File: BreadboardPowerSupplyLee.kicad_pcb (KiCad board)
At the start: 2 copper layers, 31.8 x 50.8 mm, 15 parts, among them J1 Barrel_Jack_Switch, J2 Conn_02x02_Odd_Even, J3 Conn_02x02_Odd_Even, SW1 SW_SPDT, U1 LM7805_TO220

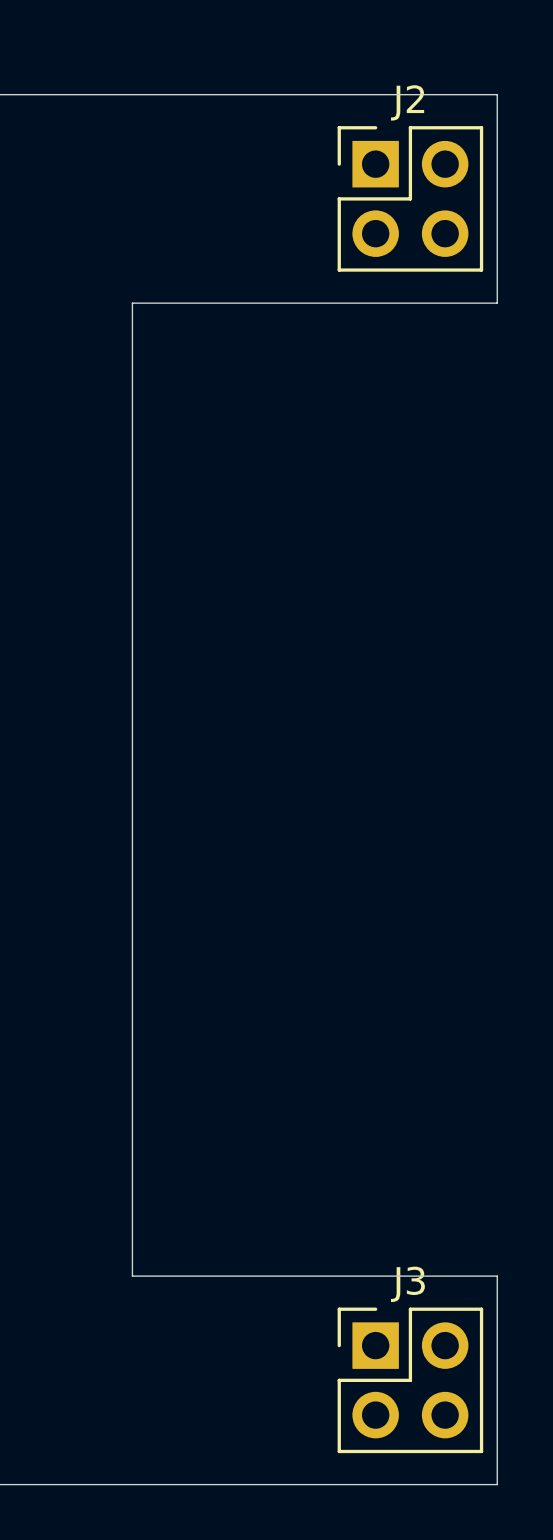
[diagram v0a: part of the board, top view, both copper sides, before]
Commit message: Place J2 and J3 1.85 inches top to bottom.
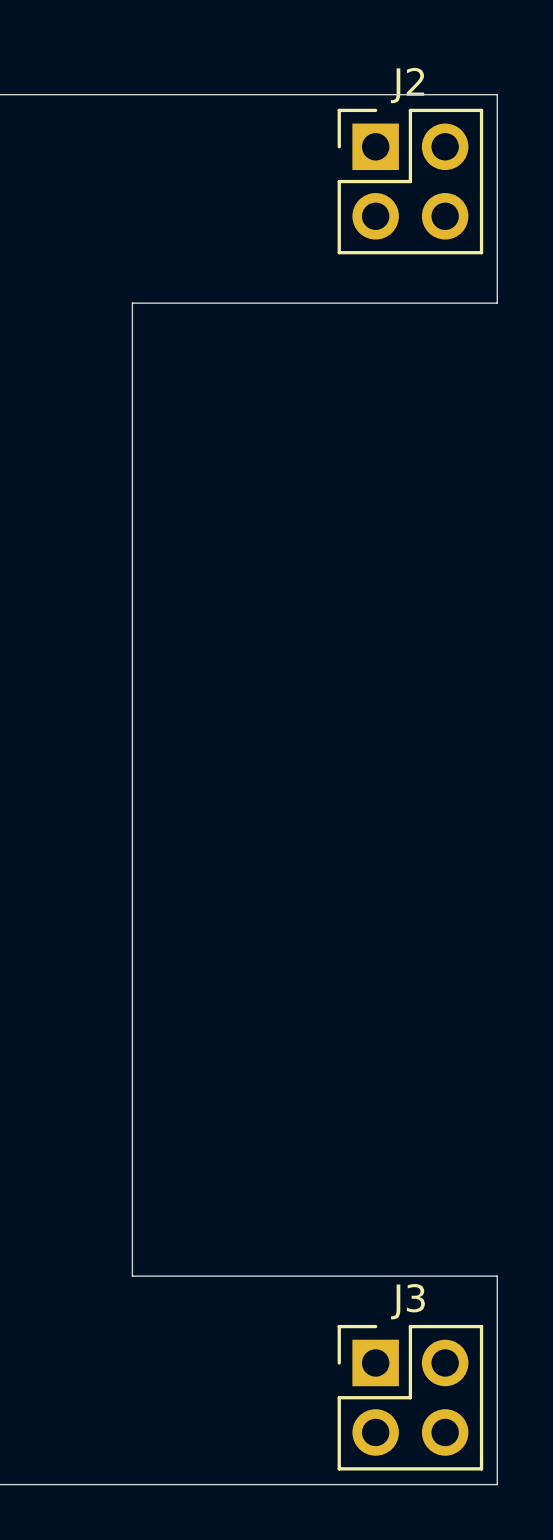
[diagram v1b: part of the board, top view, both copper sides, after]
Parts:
- moved J2 0.63 mm to (160.7, 90.8)
- moved J3 0.63 mm to (160.7, 135.3)
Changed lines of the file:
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@@
     )
   )
-  (module Connector_PinHeader_2.54mm:PinHeader_2x02_P2.54mm_Vertical (layer F.Cu)
-    (at 160.655 91.44)
+  (module Connector_PinHeader_2.54mm:PinHeader_2x02_P2.54mm_Vertical locked (layer F.Cu)
+    (at 160.655 90.805)
     (descr "Through hole straight pin header, 2x02, 2.54mm pitch, double rows")
     (tags "Through hole pin header THT 2x02 2.54mm double row")
@@
     )
   )
-  (module Connector_PinHeader_2.54mm:PinHeader_2x02_P2.54mm_Vertical (layer F.Cu)
-    (at 160.655 134.62)
+  (module Connector_PinHeader_2.54mm:PinHeader_2x02_P2.54mm_Vertical locked (layer F.Cu)
+    (at 160.655 135.255)
     (descr "Through hole straight pin header, 2x02, 2.54mm pitch, double rows")
     (tags "Through hole pin header THT 2x02 2.54mm double row")
@@
     )
   )
-  (dimension 45.72 (width 0.15) (layer Dwgs.User)
-    (gr_text "1.8000 in" (at 172.75 114.3 90) (layer Dwgs.User)
-      (effects (font (size 1 1) (thickness 0.15)))
-    )
-    (feature1 (pts (xy 160.655 91.44) (xy 172.036421 91.44)))
-    (feature2 (pts (xy 160.655 137.16) (xy 172.036421 137.16)))
-    (crossbar (pts (xy 171.45 137.16) (xy 171.45 91.44)))
-    (arrow1a (pts (xy 171.45 91.44) (xy 172.036421 92.566504)))
-    (arrow1b (pts (xy 171.45 91.44) (xy 170.863579 92.566504)))
-    (arrow2a (pts (xy 171.45 137.16) (xy 172.036421 136.033496)))
-    (arrow2b (pts (xy 171.45 137.16) (xy 170.863579 136.033496)))
-  )
-  (dimension 48.26 (width 0.15) (layer Dwgs.User)
-    (gr_text "1.9000 in" (at 116.81 115.57 90) (layer Dwgs.User)
-      (effects (font (size 1 1) (thickness 0.15)))
-    )
-    (feature1 (pts (xy 130.81 91.44) (xy 117.523579 91.44)))
+  (dimension 46.99 (width 0.15) (layer Dwgs.User)
+    (gr_text "1.8500 in" (at 172.75 114.3 90) (layer Dwgs.User)
+      (effects (font (size 1 1) (thickness 0.15)))
+    )
+    (feature1 (pts (xy 160.655 90.805) (xy 172.036421 90.805)))
+    (feature2 (pts (xy 160.655 137.795) (xy 172.036421 137.795)))
+    (crossbar (pts (xy 171.45 137.795) (xy 171.45 90.805)))
+    (arrow1a (pts (xy 171.45 90.805) (xy 172.036421 91.931504)))
+    (arrow1b (pts (xy 171.45 90.805) (xy 170.863579 91.931504)))
+    (arrow2a (pts (xy 171.45 137.795) (xy 172.036421 136.668496)))
+    (arrow2b (pts (xy 171.45 137.795) (xy 170.863579 136.668496)))
+  )
+  (dimension 50.8 (width 0.15) (layer Dwgs.User)
+    (gr_text "2.0000 in" (at 116.81 114.3 90) (layer Dwgs.User)
+      (effects (font (size 1 1) (thickness 0.15)))
+    )
+    (feature1 (pts (xy 130.81 88.9) (xy 117.523579 88.9)))
     (feature2 (pts (xy 130.81 139.7) (xy 117.523579 139.7)))
-    (crossbar (pts (xy 118.11 139.7) (xy 118.11 91.44)))
-    (arrow1a (pts (xy 118.11 91.44) (xy 118.696421 92.566504)))
-    (arrow1b (pts (xy 118.11 91.44) (xy 117.523579 92.566504)))
+    (crossbar (pts (xy 118.11 139.7) (xy 118.11 88.9)))
+    (arrow1a (pts (xy 118.11 88.9) (xy 118.696421 90.026504)))
+    (arrow1b (pts (xy 118.11 88.9) (xy 117.523579 90.026504)))
     (arrow2a (pts (xy 118.11 139.7) (xy 118.696421 138.573496)))
     (arrow2b (pts (xy 118.11 139.7) (xy 117.523579 138.573496)))
@@
     (arrow2b (pts (xy 124.46 139.7) (xy 123.873579 138.573496)))
   )
-  (dimension 5.08 (width 0.15) (layer Dwgs.User)
-    (gr_text "0.2000 in" (at 127.605 137.16 90) (layer Dwgs.User)
-      (effects (font (size 1 1) (thickness 0.15)))
-    )
-    (feature1 (pts (xy 130.81 134.62) (xy 128.318579 134.62)))
+  (dimension 4.445 (width 0.15) (layer Dwgs.User)
+    (gr_text "0.1750 in" (at 127.605 137.4775 90) (layer Dwgs.User)
+      (effects (font (size 1 1) (thickness 0.15)))
+    )
+    (feature1 (pts (xy 130.81 135.255) (xy 128.318579 135.255)))
     (feature2 (pts (xy 130.81 139.7) (xy 128.318579 139.7)))
-    (crossbar (pts (xy 128.905 139.7) (xy 128.905 134.62)))
-    (arrow1a (pts (xy 128.905 134.62) (xy 129.491421 135.746504)))
-    (arrow1b (pts (xy 128.905 134.62) (xy 128.318579 135.746504)))
+    (crossbar (pts (xy 128.905 139.7) (xy 128.905 135.255)))
+    (arrow1a (pts (xy 128.905 135.255) (xy 129.491421 136.381504)))
+    (arrow1b (pts (xy 128.905 135.255) (xy 128.318579 136.381504)))
     (arrow2a (pts (xy 128.905 139.7) (xy 129.491421 138.573496)))
     (arrow2b (pts (xy 128.905 139.7) (xy 128.318579 138.573496)))

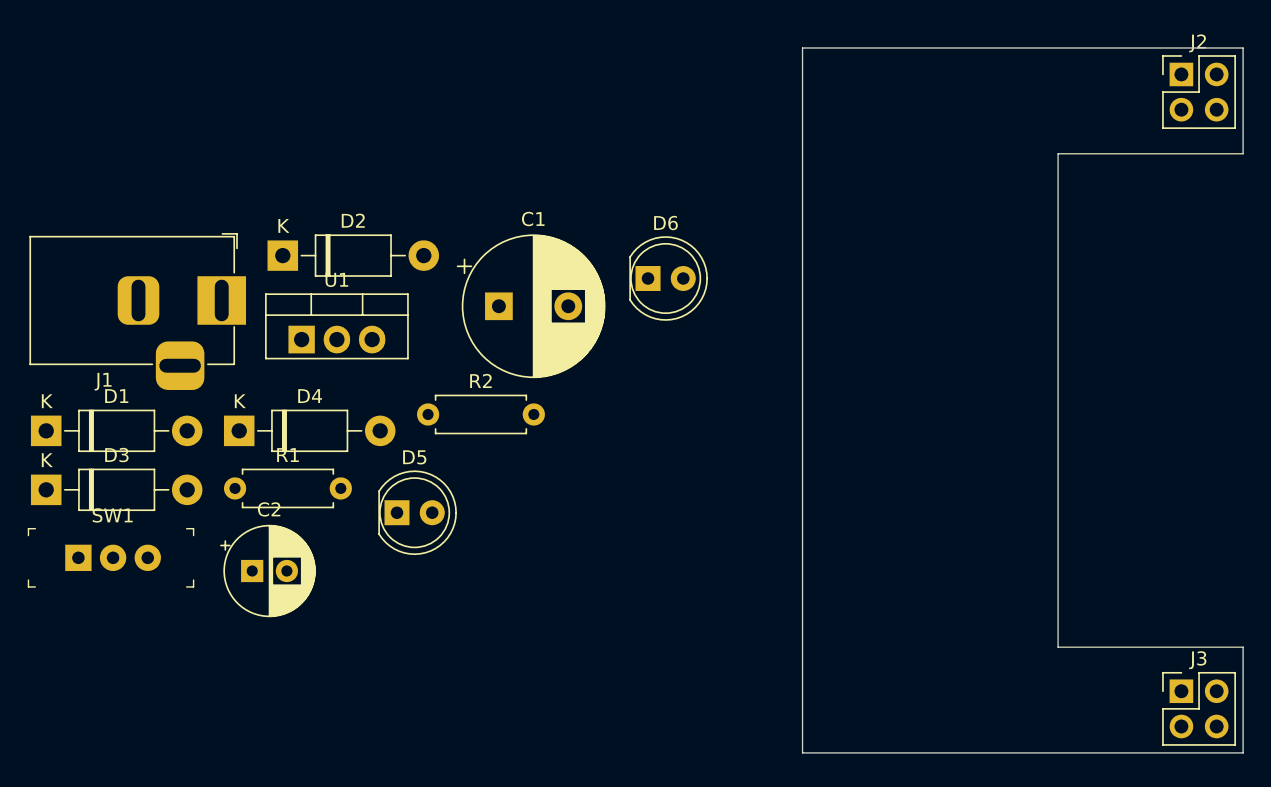
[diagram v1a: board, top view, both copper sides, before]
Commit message: Place all components in board outline.
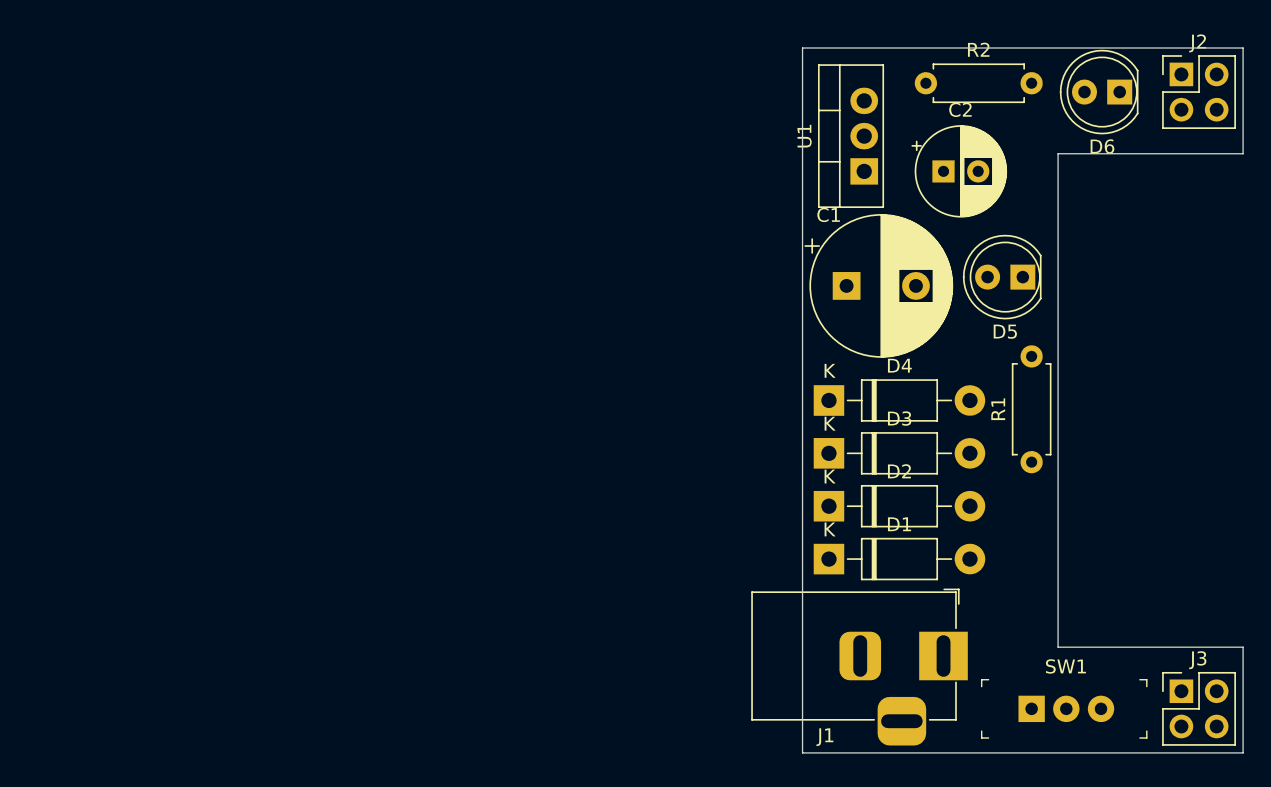
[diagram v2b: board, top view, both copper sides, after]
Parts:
- moved SW1 69.6 mm to (149.9, 136.5)
- moved J1 58.0 mm to (143.5, 132.7)
- moved C2 57.5 mm to (143.5, 97.8)
- moved R1 57.4 mm to (149.9, 118.7), turned to 90 degrees
- moved D1 57.2 mm to (135.3, 125.7)
- moved D3 56.5 mm to (135.3, 118.1)
- moved D5 48.2 mm to (149.2, 105.4), turned to 180 degrees
- moved D2 43.3 mm to (135.3, 121.9)
- moved R2 43.1 mm to (142.2, 91.4)
- moved D4 42.6 mm to (135.3, 114.3)
- moved U1 42.3 mm to (137.8, 97.8), turned to 90 degrees
- moved D6 36.6 mm to (156.2, 92.1), turned to 180 degrees
- moved C1 25.1 mm to (136.5, 106.0)

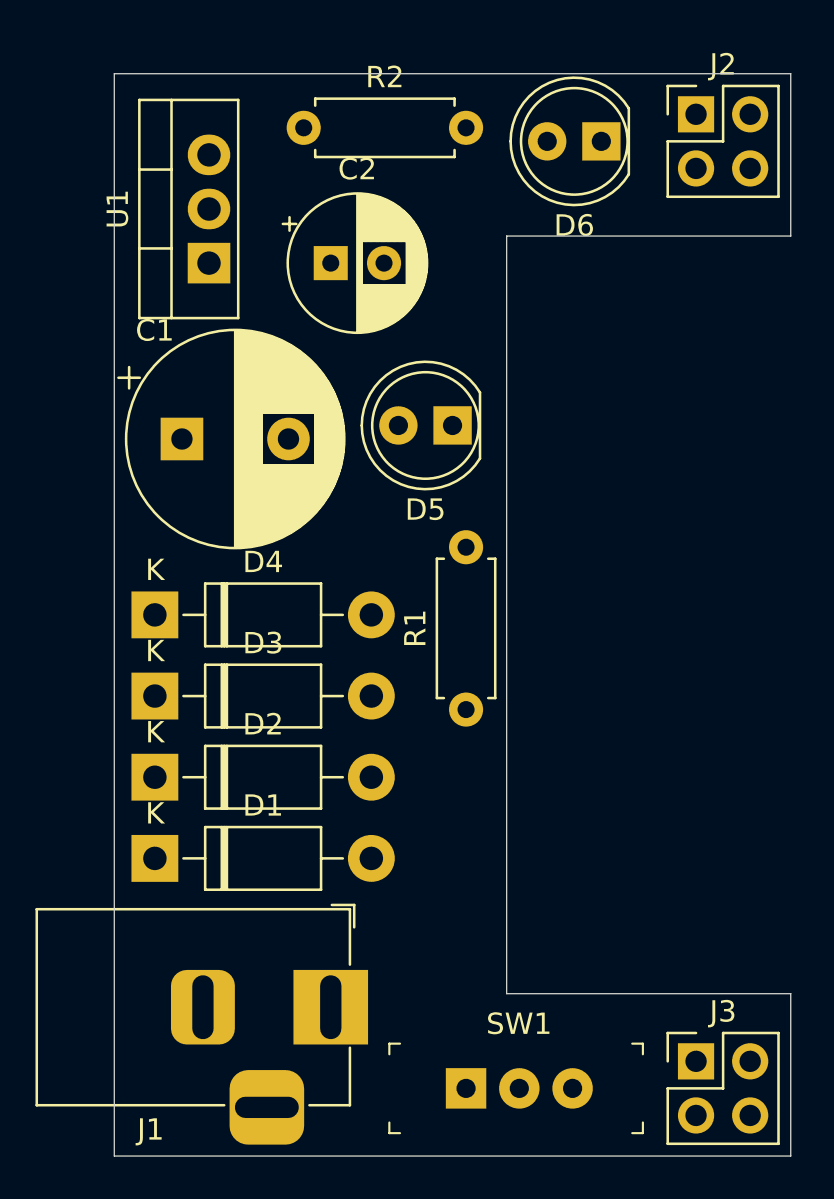
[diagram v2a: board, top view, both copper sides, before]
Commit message: Route traces. Pour ground fill on bottom.
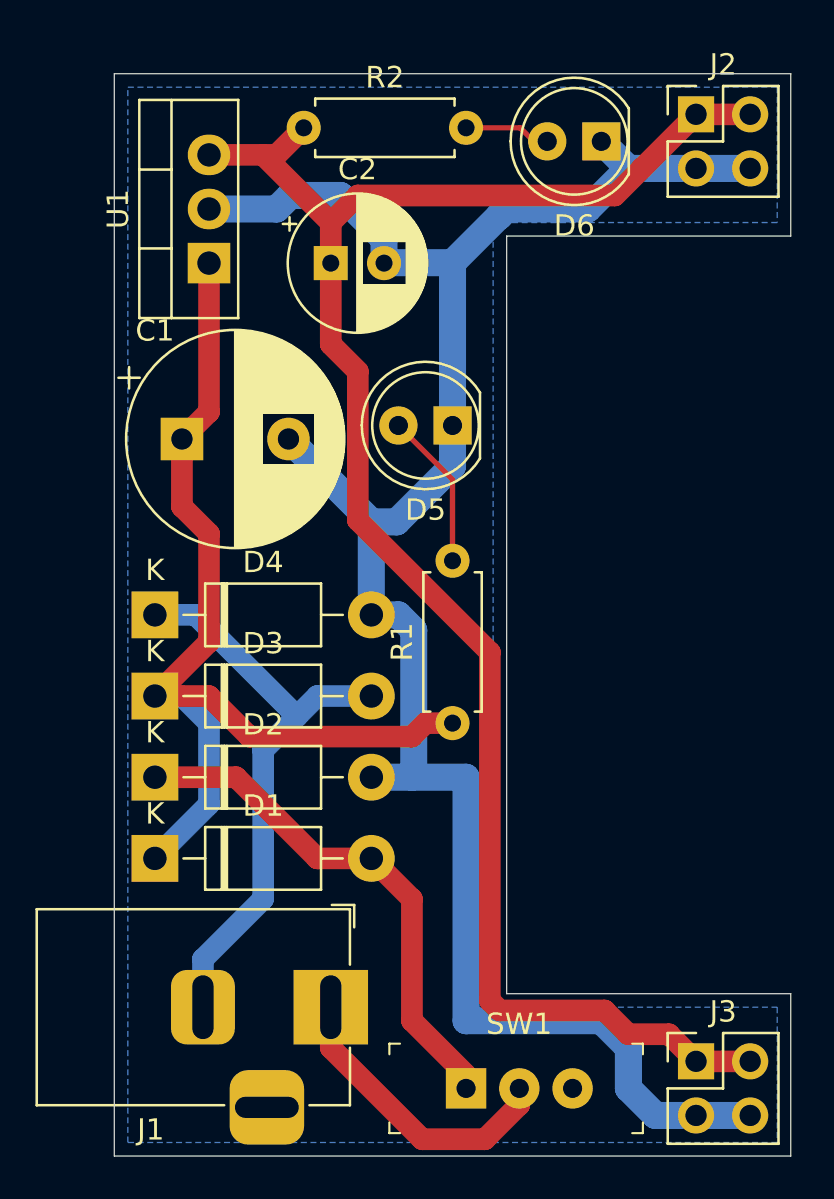
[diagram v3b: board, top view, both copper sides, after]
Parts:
- moved R1 0.90 mm to (149.2, 119.4)
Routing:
- net GND: track 0.00 -> 97.0 mm
- net /Vout: track 0.00 -> 84.3 mm
- net /VDCraw: track 0.00 -> 47.9 mm
- net /VinReference: track 0.00 -> 28.0 mm
- net /VSwitched: track 0.00 -> 24.4 mm
- net /Vin: track 0.00 -> 14.0 mm
- net /PowerOn: track 0.00 -> 7.40 mm
- net /RegOn: track 0.00 -> 4.07 mm
- added copper zone on B.Cu, net GND

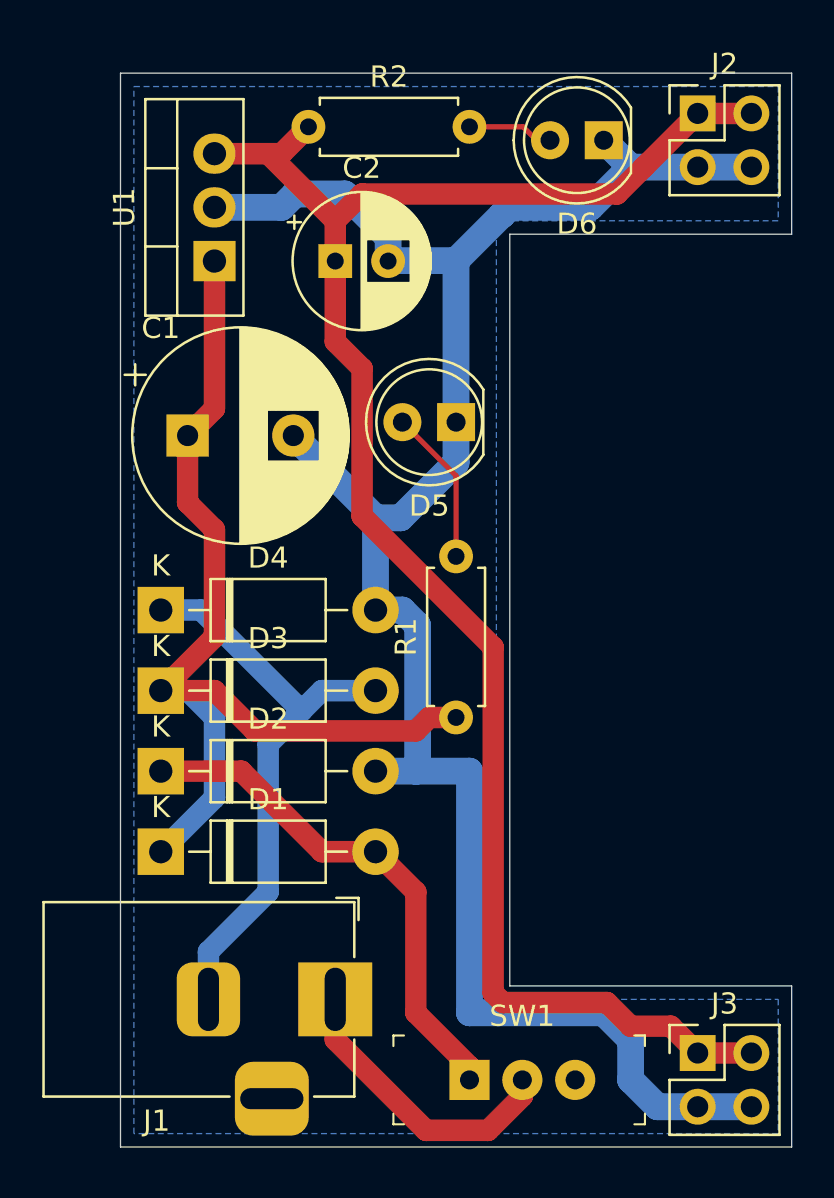
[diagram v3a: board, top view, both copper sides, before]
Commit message: Add test point for Vcc and GND in schematic and PCB. Make gerbers. Looking good.
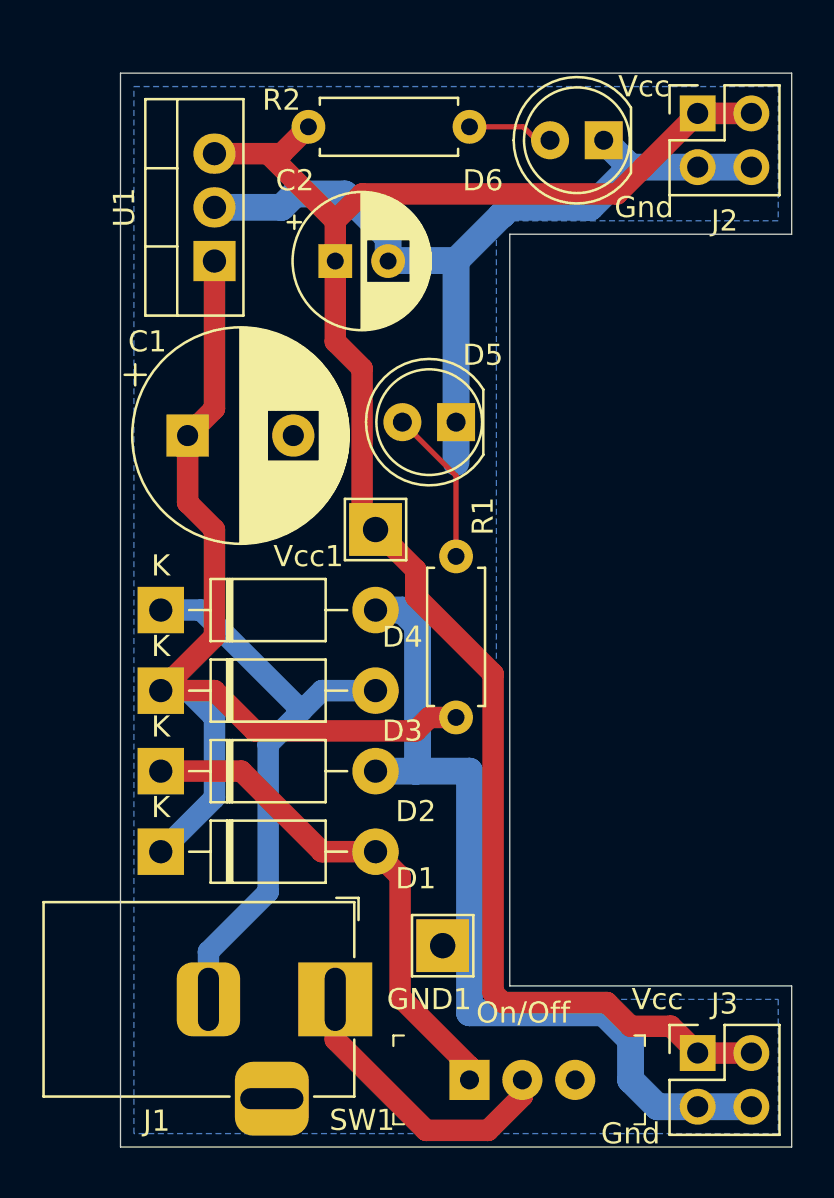
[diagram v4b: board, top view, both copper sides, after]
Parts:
- added G***: LOGO, ASlibrary:AmusedScientist5mmx5mm, B.Cu at (148.0, 101.6)
- added GND1: GND, TestPoint:TestPoint_THTPad_2.5x2.5mm_Drill1.2mm, F.Cu at (148.6, 130.2)
- added REF**: KiCad-Logo2_5mm_SilkScreen, Symbol:KiCad-Logo2_5mm_SilkScreen, B.Cu at (141.0, 109.9)
- added Vcc1: Vcc, TestPoint:TestPoint_THTPad_2.5x2.5mm_Drill1.2mm, F.Cu at (145.4, 110.5)
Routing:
- net GND: track 97.0 -> 82.2 mm
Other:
- board text added: "BreadboardPowerSupplyLee V0.0.1"
- board text added: "Gnd"
- board text added: "On/Off"
- board text added: "Vcc"
